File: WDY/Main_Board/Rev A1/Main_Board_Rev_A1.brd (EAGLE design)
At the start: 130 x 70 mm, 200 parts, among them J1 22-05-7028-02, J10 22-05-7038-03, J11 FTSH-105-01-L-DV, J12 22-05-7028-02, J13 22-05-7028-02, J14 22-05-7028-02, J15 22-05-7058-05, J16 22-27-2061-06, J17 22-05-7048-04, J2 22-05-7028-02, J3 22-05-7048-04, J4 22-05-7048-04, J5 1241050-5, J6 90814-0208, J7 90814-0206, J8 90814-0208, J9 22-05-7038-03, K1 G6K-2G-Y, K2 G6K-2G-Y, K3 G6K-2G-Y, K4 G6K-2G-Y, P1 RB1-125BAG1A, SW1 B3FS-1015, SW2 B3FS-1015, T1 MMBT2222AL, U1 LPC1768FBD100, U10 TLV313, U11 SN74LVC3G17DCTR, U2 SN74LVC3G17DCTR, U3 SN74LVC3G17DCTR, U4 TPL0401A, U5 AT24C512C-SSHM-B, U6 SN74LVC2G17DBVR, U7 SN74LVC2G17DBVR, U8 LT1767EMS8E-5PBF, U9 TC1264-3.3, X1 FC-135, X2 MSTBA2

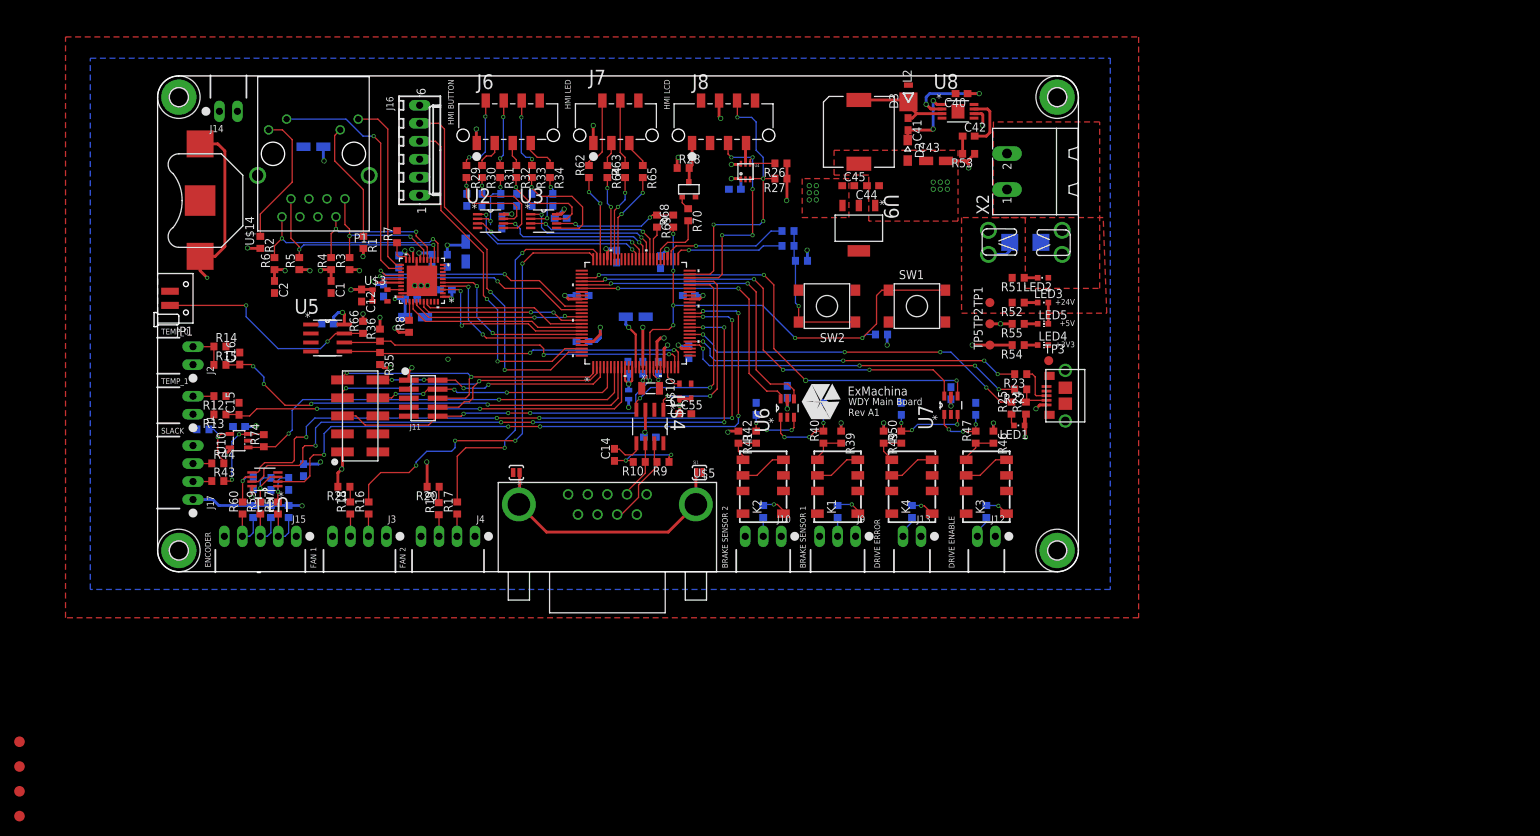
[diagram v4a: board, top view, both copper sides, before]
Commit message: Add LED value
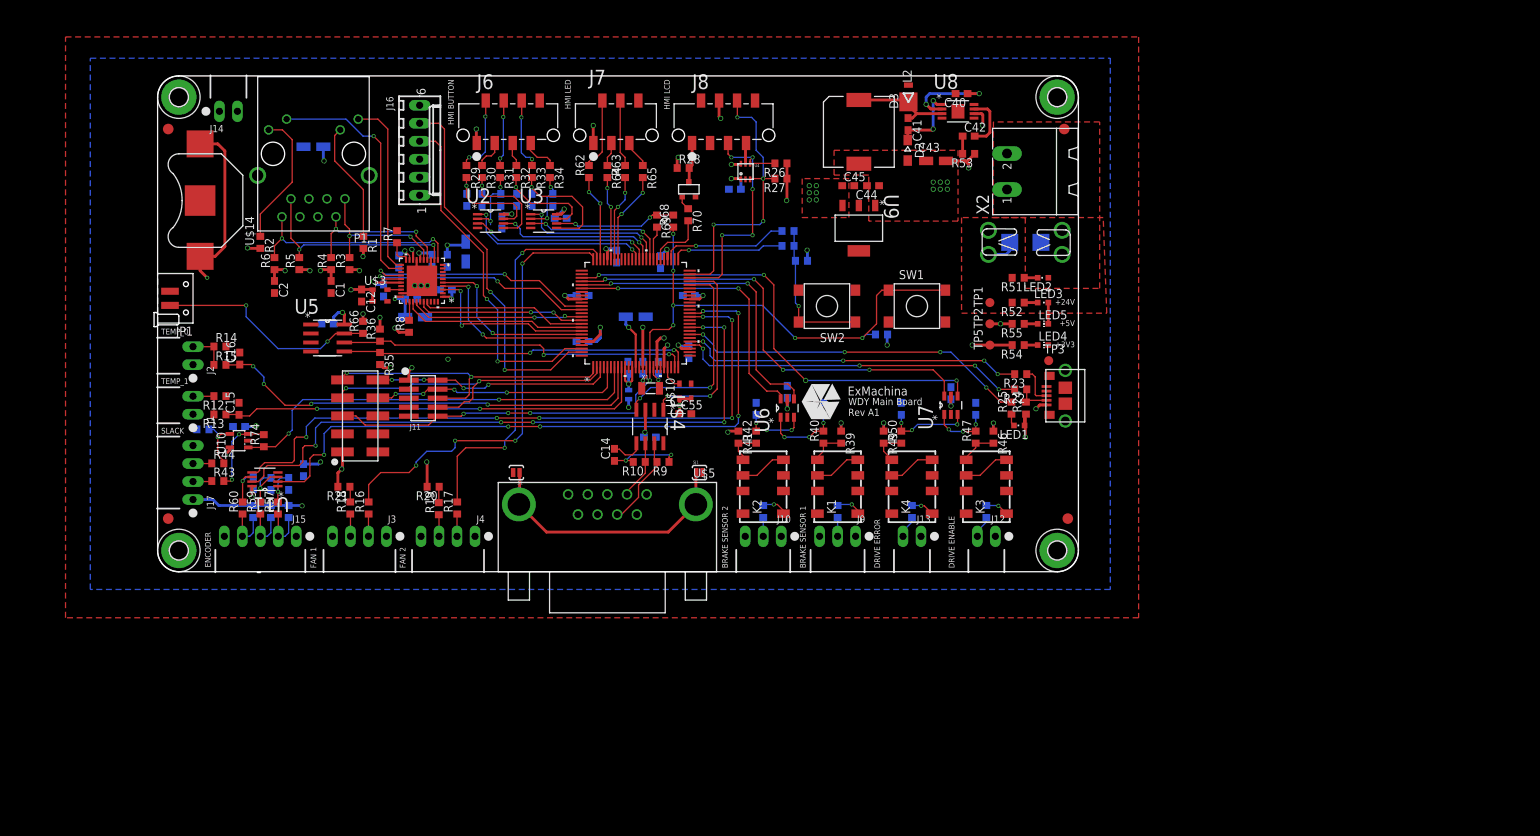
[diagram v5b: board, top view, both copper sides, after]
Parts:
- D1: value (none) -> Green
- moved JP5 176.5 mm to (128.0, 62.5)
- moved JP3 152.1 mm to (128.5, 7.50)
- moved JP4 95.8 mm to (1.50, 62.5)
- moved JP2 37.9 mm to (1.50, 7.50)
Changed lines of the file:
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@@
 <element name="R52" library="rcl" package="R0603" value="4k7" x="121.5" y="38" rot="R180"/>
 <element name="LED3" library="led" package="CHIPLED_0603" value="Red" x="125" y="38" rot="R270"/>
-<element name="D1" library="diode" package="SMB" value="" x="122.5" y="46.5" rot="MR180">
+<element name="D1" library="diode" package="SMB" value="Green" x="122.5" y="46.5" rot="MR180">
 <attribute name="OC_FARNELL" value="2341599" x="122.5" y="46.5" size="1.778" layer="28" rot="MR180" display="off"/>
 <attribute name="MP" value="STMICROELECTRONICS" x="122.5" y="46.5" size="1.778" layer="28" rot="MR180" display="off"/>
@@
 <element name="C24" library="rcl" package="C0603" value="0.1uF" x="11.5" y="20.5" rot="MR0"/>
 <element name="J11" library="con-samtec" package="FTSH-105-01-L-DV" value="FTSH-105-01-L-DV" x="37.5" y="24.5" rot="R270"/>
-<element name="JP2" library="SparkFun" package="FIDUCIAL-1.5X3" value="FIDUCIAL1.5X3" x="-19.5" y="-24"/>
-<element name="JP3" library="SparkFun" package="FIDUCIAL-1.5X3" value="FIDUCIAL1.5X3" x="-19.5" y="-27.5"/>
-<element name="JP4" library="SparkFun" package="FIDUCIAL-1.5X3" value="FIDUCIAL1.5X3" x="-19.5" y="-31"/>
-<element name="JP5" library="SparkFun" package="FIDUCIAL-1.5X3" value="FIDUCIAL1.5X3" x="-19.5" y="-34.5"/>
+<element name="JP2" library="SparkFun" package="FIDUCIAL-1.5X3" value="FIDUCIAL1.5X3" x="1.5" y="7.5"/>
+<element name="JP3" library="SparkFun" package="FIDUCIAL-1.5X3" value="FIDUCIAL1.5X3" x="128.5" y="7.5"/>
+<element name="JP4" library="SparkFun" package="FIDUCIAL-1.5X3" value="FIDUCIAL1.5X3" x="1.5" y="62.5"/>
+<element name="JP5" library="SparkFun" package="FIDUCIAL-1.5X3" value="FIDUCIAL1.5X3" x="128" y="62.5"/>
 </elements>
 <signals>

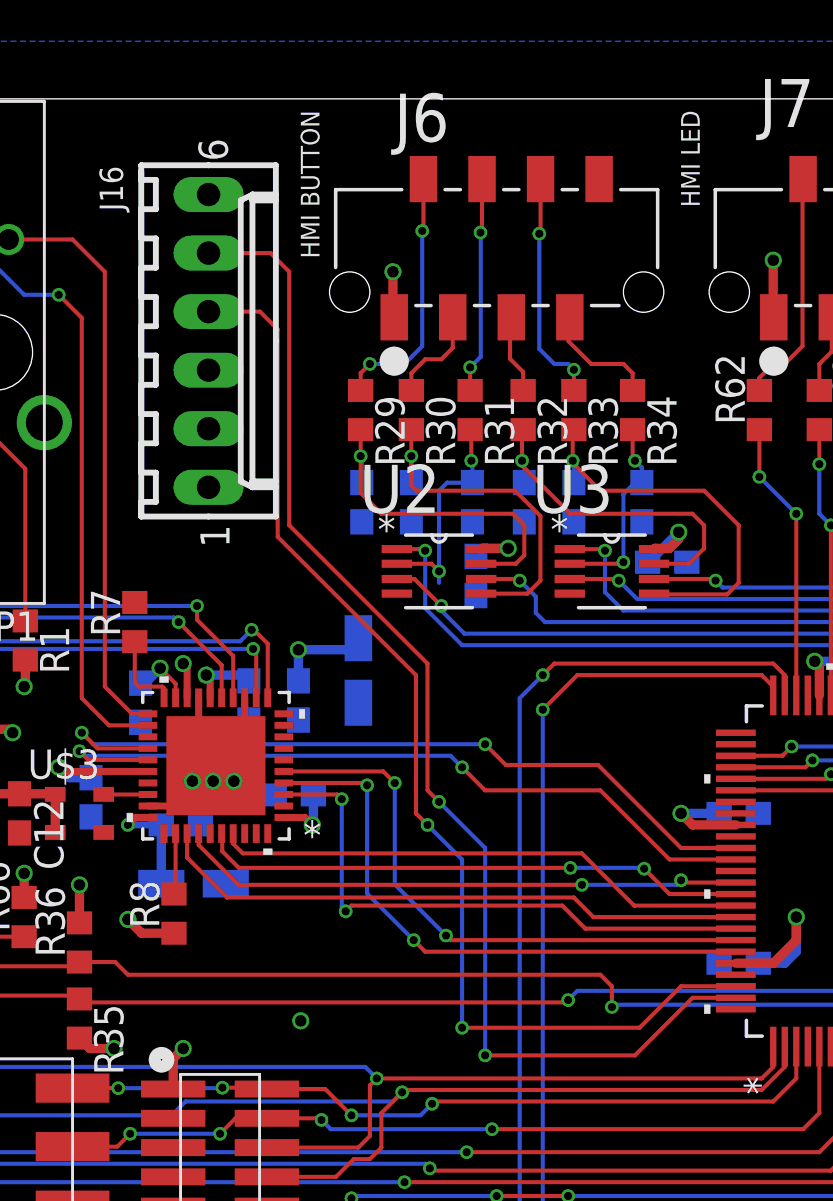
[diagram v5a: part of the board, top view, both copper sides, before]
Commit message: Update Main_Board_Rev_A1 schematics and board and con-molex lib
* Add solder jumper to +5V supplied by UART
* Swap TXDO and RXDO UART signals
* Simplify 22-27-2061-06 package in con-molex.lbr
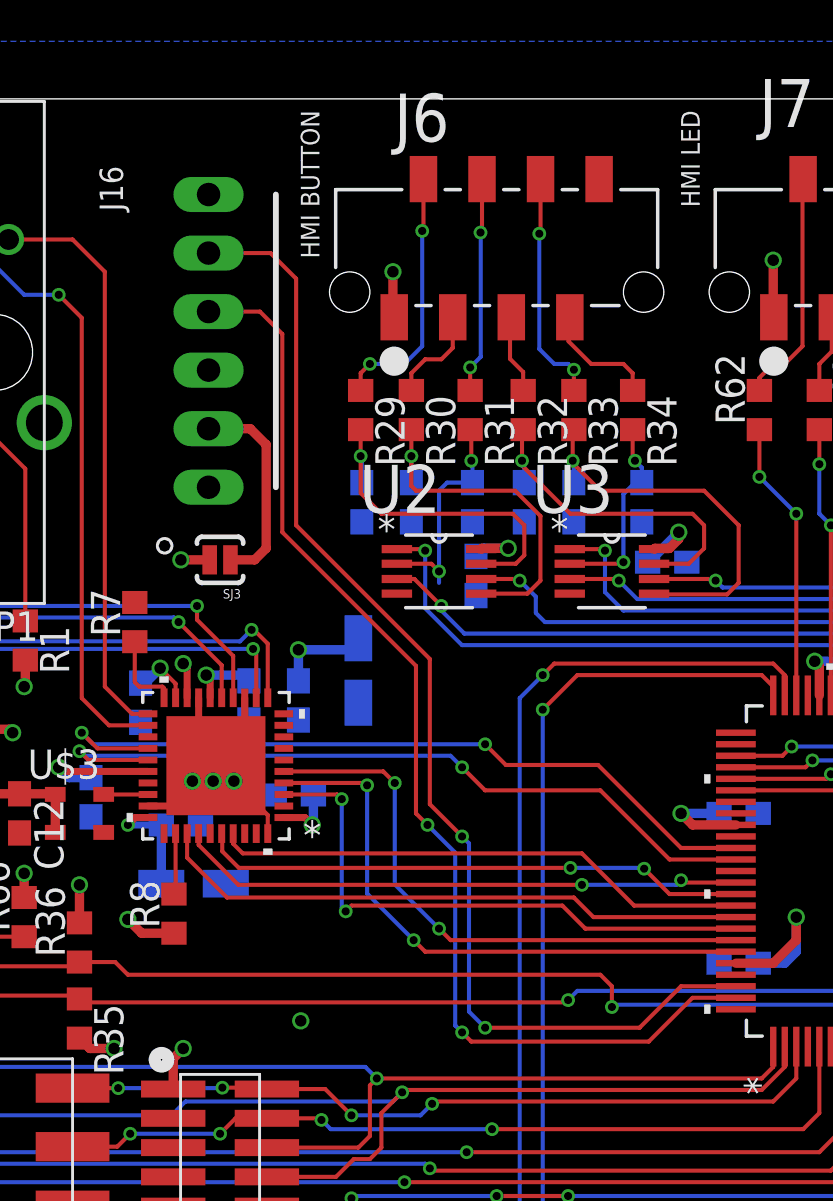
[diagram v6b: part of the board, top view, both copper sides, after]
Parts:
- added SJ3: SOLDERJUMPERNO, SparkFun-Passives:SJ_2S-NO
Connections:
- new net N$69: J16.2, SJ3.1
- net +5V: now also SJ3.2; no longer J16.2
- net ISP_RXDO: now also J16.4; no longer J16.5
- net ISP_TXDO: now also J16.5; no longer J16.4
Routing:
- net N$69: track 0.00 -> 9.04 mm
- net +5V: track 121.9 -> 127.3 mm, vias 17 -> 18
- net GND: track 19.8 -> 23.5 mm
- net ISP_RXDO: track 53.3 -> 50.0 mm
- net ISP_TXDO: track 49.6 -> 51.8 mm
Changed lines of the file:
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@@
 <element name="JP4" library="SparkFun" package="FIDUCIAL-1.5X3" value="FIDUCIAL1.5X3" x="1.5" y="62.5"/>
 <element name="JP5" library="SparkFun" package="FIDUCIAL-1.5X3" value="FIDUCIAL1.5X3" x="128" y="62.5"/>
+<element name="SJ3" library="SparkFun-Passives" package="SJ_2S-NO" value="SOLDERJUMPERNO" x="37.5" y="50" rot="R180"/>
 </elements>
 <signals>
@@
 <contactref element="J11" pad="5"/>
 <contactref element="J11" pad="9"/>
+<wire x1="39.57" y1="38.1236" x2="39.57" y2="38.93" width="0.1778" layer="1"/>
+<wire x1="39.57" y1="38.93" x2="39" y2="39.5" width="0.1778" layer="1"/>
+<wire x1="39.57" y1="38.93" x2="38.1" y2="40.4" width="0.15" layer="1"/>
 </signal>
 <signal name="+3V3" class="2">
@@
 <wire x1="40.2664" y1="40.82" x2="44.58" y2="40.82" width="0.1778" layer="1"/>
 <wire x1="44.58" y1="40.82" x2="45.08" y2="40.32" width="0.1778" layer="1"/>
-<via x="47.3" y="33.7" extent="1-16" drill="0.35"/>
-<wire x1="47.3" y1="33.7" x2="47.5" y2="33.5" width="0.1778" layer="1"/>
+<via x="47" y="34" extent="1-16" drill="0.35"/>
+<wire x1="47" y1="34" x2="47.5" y2="33.5" width="0.1778" layer="1"/>
 <wire x1="45.08" y1="35.92" x2="45.08" y2="40.32" width="0.1778" layer="16"/>
-<wire x1="47.3" y1="33.7" x2="45.08" y2="35.92" width="0.1778" layer="16"/>
+<wire x1="47" y1="34" x2="45.08" y2="35.92" width="0.1778" layer="16"/>
 </signal>
 <signal name="ETH_RXD_N" class="1">
@@
 <signal name="ISP_RXDO" class="1">
 <contactref element="U1" pad="99"/>
+<wire x1="40.2" y1="51.2" x2="46" y2="45.4" width="0.1778" layer="1"/>
+<wire x1="59.88" y1="31" x2="58" y2="31" width="0.1778" layer="1"/>
+<wire x1="58" y1="31" x2="56.1" y2="29.1" width="0.1778" layer="1"/>
+<wire x1="56.1" y1="29.1" x2="48.4" y2="29.1" width="0.1778" layer="1"/>
+<wire x1="48.4" y1="29.1" x2="48" y2="29.5" width="0.1778" layer="1"/>
+<via x="48" y="29.5" extent="1-16" drill="0.35"/>
+<wire x1="48" y1="29.5" x2="47.7" y2="29.8" width="0.1778" layer="16"/>
+<wire x1="47.7" y1="29.8" x2="47.7" y2="37.3" width="0.1778" layer="16"/>
+<via x="46.5" y="38.5" extent="1-16" drill="0.35"/>
+<wire x1="46.5" y1="38.5" x2="46" y2="39" width="0.1778" layer="1"/>
+<wire x1="46" y1="39" x2="46" y2="45.4" width="0.1778" layer="1"/>
+<contactref element="J16" pad="4"/>
+<wire x1="40.2" y1="51.2" x2="40.2" y2="59.8" width="0.1778" layer="1"/>
+<wire x1="40.2" y1="59.8" x2="39.23" y2="60.77" width="0.1778" layer="1"/>
+<wire x1="39.23" y1="60.77" x2="37" y2="60.77" width="0.1778" layer="1"/>
+<wire x1="47.7" y1="37.3" x2="46.5" y2="38.5" width="0.1778" layer="16"/>
+</signal>
+<signal name="ISP_TXDO" class="1">
+<contactref element="U1" pad="98"/>
+<wire x1="40.8" y1="51.5" x2="46.6" y2="45.7" width="0.1778" layer="1"/>
+<wire x1="59.88" y1="31.5" x2="57.5" y2="31.5" width="0.1778" layer="1"/>
+<wire x1="57.5" y1="31.5" x2="55.7" y2="29.7" width="0.1778" layer="1"/>
+<wire x1="55.7" y1="29.7" x2="49" y2="29.7" width="0.1778" layer="1"/>
+<via x="49" y="29.7" extent="1-16" drill="0.35"/>
+<via x="48" y="38" extent="1-16" drill="0.35"/>
+<wire x1="46.6" y1="39.4" x2="46.6" y2="45.7" width="0.1778" layer="1"/>
+<wire x1="49" y1="29.7" x2="48.3" y2="30.4" width="0.1778" layer="16"/>
+<wire x1="48.3" y1="30.4" x2="48.3" y2="37.7" width="0.1778" layer="16"/>
+<wire x1="48.3" y1="37.7" x2="48" y2="38" width="0.1778" layer="16"/>
 <contactref element="J16" pad="5"/>
 <wire x1="37" y1="63.31" x2="39.69" y2="63.31" width="0.1778" layer="1"/>
-<wire x1="39.69" y1="63.31" x2="40.5" y2="62.5" width="0.1778" layer="1"/>
-<wire x1="40.5" y1="62.5" x2="40.5" y2="51.5" width="0.1778" layer="1"/>
-<wire x1="40.5" y1="51.5" x2="46.5" y2="45.5" width="0.1778" layer="1"/>
-<wire x1="59.88" y1="31" x2="58" y2="31" width="0.1778" layer="1"/>
-<wire x1="58" y1="31" x2="55.5" y2="28.5" width="0.1778" layer="1"/>
-<wire x1="55.5" y1="28.5" x2="49" y2="28.5" width="0.1778" layer="1"/>
-<via x="49" y="28.5" extent="1-16" drill="0.35"/>
-<wire x1="49" y1="28.5" x2="49" y2="37.5" width="0.1778" layer="16"/>
-<wire x1="49" y1="37.5" x2="47" y2="39.5" width="0.1778" layer="16"/>
-<via x="47" y="39.5" extent="1-16" drill="0.35"/>
-<wire x1="47" y1="39.5" x2="46.5" y2="40" width="0.1778" layer="1"/>
-<wire x1="46.5" y1="40" x2="46.5" y2="45.5" width="0.1778" layer="1"/>
-</signal>
-<signal name="ISP_TXDO" class="1">
-<contactref element="U1" pad="98"/>
-<contactref element="J16" pad="4"/>
-<wire x1="37" y1="60.77" x2="39.23" y2="60.77" width="0.1778" layer="1"/>
-<wire x1="39.23" y1="60.77" x2="40" y2="60" width="0.1778" layer="1"/>
-<wire x1="40" y1="60" x2="40" y2="51" width="0.1778" layer="1"/>
-<wire x1="40" y1="51" x2="46" y2="45" width="0.1778" layer="1"/>
-<wire x1="59.88" y1="31.5" x2="57.5" y2="31.5" width="0.1778" layer="1"/>
-<wire x1="57.5" y1="31.5" x2="55.7" y2="29.7" width="0.1778" layer="1"/>
-<wire x1="55.7" y1="29.7" x2="48" y2="29.7" width="0.1778" layer="1"/>
-<via x="48" y="29.7" extent="1-16" drill="0.35"/>
-<via x="46.5" y="38.5" extent="1-16" drill="0.35"/>
-<wire x1="46.5" y1="38.5" x2="46" y2="39" width="0.1778" layer="1"/>
-<wire x1="46" y1="39" x2="46" y2="45" width="0.1778" layer="1"/>
-<wire x1="48" y1="29.7" x2="48" y2="37" width="0.1778" layer="16"/>
-<wire x1="48" y1="37" x2="46.5" y2="38.5" width="0.1778" layer="16"/>
+<wire x1="39.69" y1="63.31" x2="40.8" y2="62.2" width="0.1778" layer="1"/>
+<wire x1="40.8" y1="62.2" x2="40.8" y2="51.5" width="0.1778" layer="1"/>
+<wire x1="46.6" y1="39.4" x2="48" y2="38" width="0.1778" layer="1"/>
 </signal>
 <signal name="HMI_BUTTON_2" class="1">
@@
 <wire x1="8.73" y1="66.73" x2="10" y2="68" width="0.4064" layer="3"/>
 <wire x1="10" y1="68" x2="34.5" y2="68" width="0.4064" layer="3"/>
-<contactref element="J16" pad="2"/>
 <wire x1="34.5" y1="68" x2="74" y2="68" width="0.4064" layer="3"/>
-<wire x1="37" y1="55.69" x2="35.31" y2="55.69" width="0.4064" layer="3"/>
-<wire x1="35.31" y1="55.69" x2="34.5" y2="56.5" width="0.4064" layer="3"/>
-<wire x1="34.5" y1="56.5" x2="34.5" y2="68" width="0.4064" layer="3"/>
+<wire x1="35.8" y1="50" x2="34.5" y2="51.3" width="0.4064" layer="3"/>
+<wire x1="34.5" y1="51.3" x2="34.5" y2="68" width="0.4064" layer="3"/>
 <wire x1="79.5" y1="64" x2="79.265" y2="64.235" width="0.4064" layer="1"/>
 <wire x1="79.265" y1="64.235" x2="79.265" y2="66.5194" width="0.4064" layer="1"/>
@@
 <wire x1="7.81" y1="10.19" x2="8.65" y2="9.35" width="0.4064" layer="16"/>
 <wire x1="8.65" y1="9.35" x2="13.5" y2="9.35" width="0.4064" layer="16"/>
+<contactref element="SJ3" pad="2"/>
+<via x="35.8" y="50" extent="1-16" drill="0.5"/>
+<wire x1="35.8" y1="50" x2="37.05" y2="50" width="0.4064" layer="1"/>
 </signal>
 <signal name="EEPROM_SDA">
@@
 <wire x1="7.62" y1="15.27" x2="7.65" y2="15.3" width="0.1778" layer="1"/>
 </signal>
+<signal name="N$69">
+<contactref element="SJ3" pad="1"/>
+<contactref element="J16" pad="2"/>
+<wire x1="37" y1="55.69" x2="38.81" y2="55.69" width="0.4064" layer="1"/>
+<wire x1="38.81" y1="55.69" x2="39.5" y2="55" width="0.4064" layer="1"/>
+<wire x1="39.5" y1="55" x2="39.5" y2="50.5" width="0.4064" layer="1"/>
+<wire x1="39.5" y1="50.5" x2="39" y2="50" width="0.4064" layer="1"/>
+<wire x1="39" y1="50" x2="37.95" y2="50" width="0.4064" layer="1"/>
+</signal>
 </signals>

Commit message: Connect CAN_GND to GND
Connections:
- removed net CAN_GND: U$5.3
- net GND: now also U$5.3
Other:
- board text added: "CANOPEN BUS"
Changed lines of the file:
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@@
 <layers>
 <layer number="1" name="Top" color="4" fill="1" visible="yes" active="yes"/>
-<layer number="2" name="Route2" color="6" fill="1" visible="yes" active="yes"/>
+<layer number="2" name="Route2" color="6" fill="1" visible="no" active="yes"/>
 <layer number="3" name="Route3" color="20" fill="1" visible="no" active="yes"/>
 <layer number="14" name="Route14" color="1" fill="6" visible="no" active="no"/>
@@
 <layer number="38" name="bTest" color="7" fill="1" visible="no" active="yes"/>
 <layer number="39" name="tKeepout" color="4" fill="11" visible="yes" active="yes"/>
-<layer number="40" name="bKeepout" color="1" fill="11" visible="yes" active="yes"/>
-<layer number="41" name="tRestrict" color="4" fill="10" visible="yes" active="yes"/>
-<layer number="42" name="bRestrict" color="1" fill="10" visible="yes" active="yes"/>
-<layer number="43" name="vRestrict" color="2" fill="10" visible="yes" active="yes"/>
+<layer number="40" name="bKeepout" color="1" fill="11" visible="no" active="yes"/>
+<layer number="41" name="tRestrict" color="4" fill="10" visible="no" active="yes"/>
+<layer number="42" name="bRestrict" color="1" fill="10" visible="no" active="yes"/>
+<layer number="43" name="vRestrict" color="2" fill="10" visible="no" active="yes"/>
 <layer number="44" name="Drills" color="7" fill="1" visible="no" active="yes"/>
 <layer number="45" name="Holes" color="7" fill="1" visible="no" active="yes"/>
@@
 <text x="97.5" y="22" size="1.016" layer="21">WDY Main Board
 Rev A1</text>
+<text x="52.5" y="13" size="0.8128" layer="21">CANOPEN BUS</text>
 </plain>
 <attributes>
@@
 <wire x1="39.57" y1="38.93" x2="39" y2="39.5" width="0.1778" layer="1"/>
 <wire x1="39.57" y1="38.93" x2="38.1" y2="40.4" width="0.15" layer="1"/>
+<contactref element="U$5" pad="3"/>
 </signal>
 <signal name="+3V3" class="2">
@@
 <wire x1="64.55" y1="15.7" x2="64.5" y2="15.65" width="0.1778" layer="1"/>
 </signal>
-<signal name="CAN_GND">
-<contactref element="U$5" pad="3"/>
-</signal>
 <signal name="CAN_SHLD">
